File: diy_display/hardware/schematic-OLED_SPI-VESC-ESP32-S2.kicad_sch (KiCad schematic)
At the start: 6 parts, among them J2 Connector_1

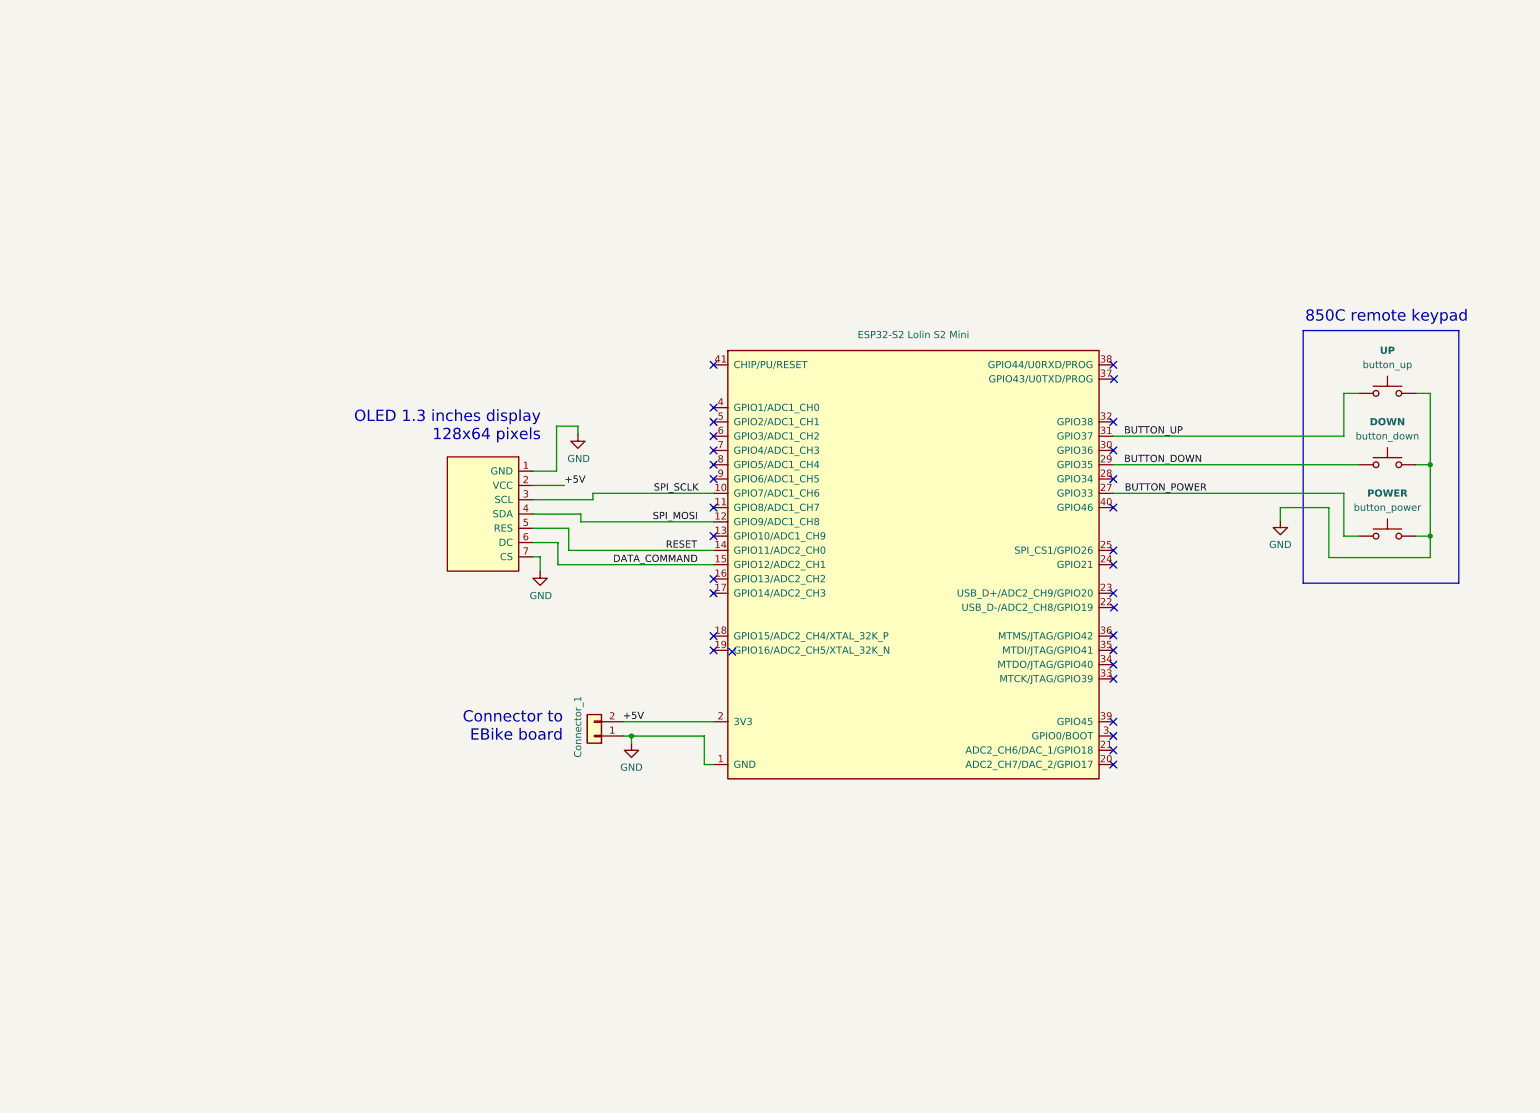
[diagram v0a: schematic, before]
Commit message: updated DIY display schematic to add low pass filters on buttons signals, to avoid noise and so false buttons clicks
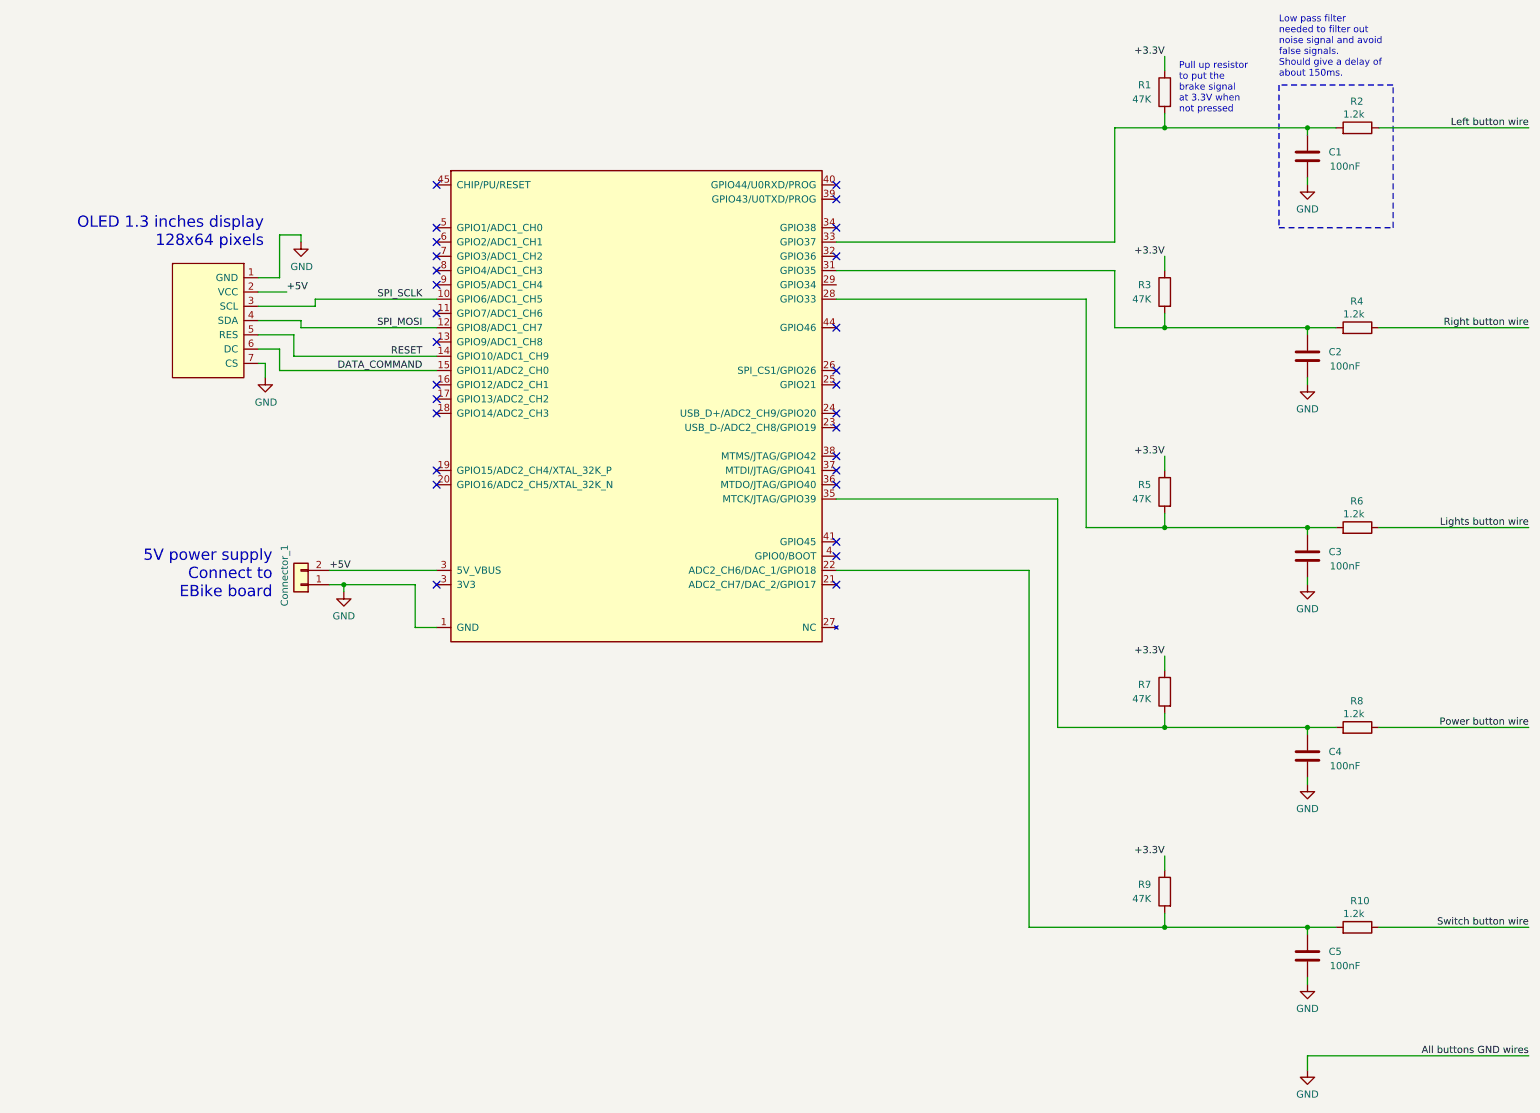
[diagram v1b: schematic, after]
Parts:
- removed J2: Connector_1, symbol Connector_Generic:Conn_01x02
- removed NA?: OLED_1.3_inches_128x64, symbol schematic-OLED_SPI-Bafang_M500_M600-rescue:SSD1306-SPI-OLED-schematic-rescue
- removed U?: ESP32-S2 Lolin S2 Mini, Espressif:ESP32-S2-WROOM, symbol Espressif:ESP32-S2-WROOM
- removed button_down: DOWN, symbol schematic-OLED_SPI-Bafang_M500_M600-rescue:Switch_SW_Push-Wired_remote
- removed button_power: POWER, symbol schematic-OLED_SPI-Bafang_M500_M600-rescue:Switch_SW_Push-Wired_remote
- removed button_up: UP, symbol schematic-OLED_SPI-Bafang_M500_M600-rescue:Switch_SW_Push-Wired_remote
- added C1, C2, C3, C4, C5: 100nF, symbol Device:C
- added J1: Connector_1, symbol Connector_Generic:Conn_01x02
- added NA1: OLED_1.3_inches_128x64, symbol schematic-OLED_SPI-Bafang_M500_M600-rescue:SSD1306-SPI-OLED-schematic-rescue
- added R1, R3, R5, R7, R9: 47K, symbol Device:R
- added R10, R2, R4, R6, R8: 1.2k, symbol Device:R
- added U1: (no value), Espressif:ESP32-S2-MINI-1, symbol Espressif:ESP32-S2-MINI-1
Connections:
- net +5V: now also J1.2 (Pin_2), NA1.2 (VCC), U1.3 (5V_VBUS)
- net DATA_COMMAND: now also NA1.6 (DC), U1.15 (GPIO11/ADC2_CH0)
- net GND: now also C1.2, C2.2, C3.2, C4.2, C5.2, J1.1 (Pin_1), NA1.1 (GND), NA1.7 (CS), U1.1 (GND), U1.2 (GND), U1.30 (GND), U1.42 (GND), U1.43 (GND), U1.46 (GND), U1.47 (GND), U1.48 (GND), U1.49 (GND), U1.50 (GND), U1.51 (GND), U1.52 (GND), U1.53 (GND), U1.54 (GND), U1.55 (GND), U1.56 (GND), U1.57 (GND), U1.58 (GND), U1.59 (GND), U1.60 (GND), U1.61 (GND), U1.62 (GND), U1.63 (GND), U1.64 (GND), U1.65 (GND)
- net RESET: now also NA1.5 (RES), U1.14 (GPIO10/ADC1_CH9)
- net SPI_MOSI: now also NA1.4 (SDA), U1.12 (GPIO8/ADC1_CH7)
- net SPI_SCLK: now also NA1.3 (SCL), U1.10 (GPIO6/ADC1_CH5)
- new net: C5.1, R10.2, R9.2, U1.22 (ADC2_CH6/DAC_1/GPIO18)
- new net: C2.1, R3.2, R4.2, U1.31 (GPIO35)
- new net: C1.1, R1.2, R2.2, U1.33 (GPIO37)
- new net: C4.1, R7.2, R8.2, U1.35 (MTCK/JTAG/GPIO39)
- new net: C3.1, R5.2, R6.2, U1.28 (GPIO33)
- new net +3.3V: R1.1, R3.1, R5.1, R7.1, R9.1
- new net Left button wire: R2.1
- new net Lights button wire: R6.1
- new net Power button wire: R8.1
- new net Right button wire: R4.1
- new net Switch button wire: R10.1
- no-connect marks 32 -> 29
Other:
- note added: "5V power supply Connect to EBike board"
- note added: "Low pass filter needed to filter out noise signal and avoid false signals. Should give a delay of about 150ms."
- note added: "Pull up resistor to put the brake signal at 3.3V when not pressed"
- note removed: "850C remote keypad"
- note removed: "Connector to EBike board"
